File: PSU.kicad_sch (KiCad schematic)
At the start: 1 part, among them U1 IRM-01-3.3

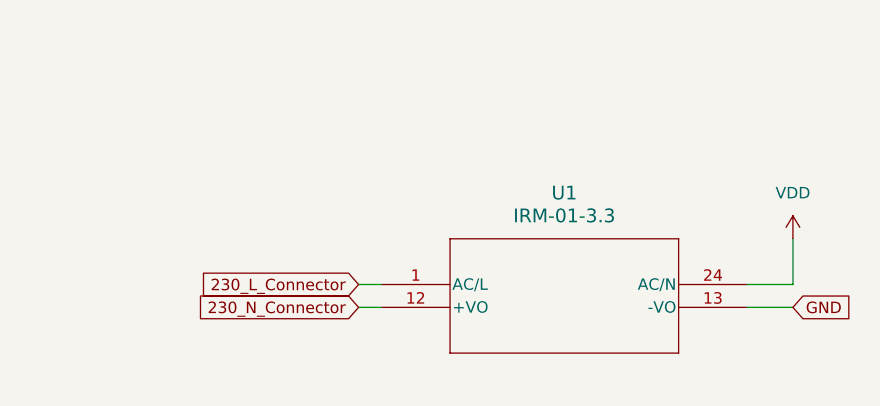
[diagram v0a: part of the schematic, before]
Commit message: Dodanie footprintów
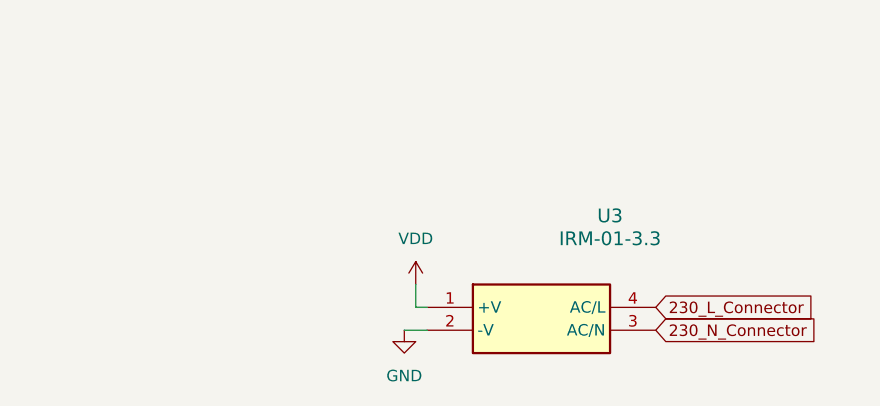
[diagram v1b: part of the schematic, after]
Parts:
- U3: renamed from U1; footprint IRM02_MWU -> Sterownik_roletyLibrary:IRM015; symbol IRM-01-3.3:IRM-01-3.3 -> IRM-01-3_3:IRM-01-3.3; Height (none) -> 15; Manufacturer_Name (none) -> Mean Well; Manufacturer_Part_Number (none) -> IRM-01-3.3; Mouser Part Number (none) -> 709-IRM01-3.3; Mouser Price/Stock (none) -> https://www.mouser.co.uk/ProductDetail/MEAN-WELL/IRM-01-3.3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
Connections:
- net 230_L_Connector: now also U3.4 (AC/L); no longer U3.1 (AC/L)
- net 230_N_Connector: now also U3.3 (AC/N); no longer U3.12 (+VO)
- net GND: now also U3.2 (-V); no longer U3.13 (-VO)
- net VDD: now also U3.1 (+V); no longer U3.24 (AC/N)
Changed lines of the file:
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@@
 	(wire
 		(pts
-			(xy 158.75 91.44) (xy 163.83 91.44)
+			(xy 123.19 93.98) (xy 121.92 93.98)
 		)
 		(stroke
@@
 	(wire
 		(pts
-			(xy 115.57 91.44) (xy 118.11 91.44)
+			(xy 121.92 93.98) (xy 121.92 91.44)
 		)
 		(stroke
@@
 	(wire
 		(pts
-			(xy 163.83 91.44) (xy 163.83 86.36)
-		)
-		(stroke
-			(width 0)
-			(type default)
-		)
-	)
-	(wire
-		(pts
-			(xy 115.57 93.98) (xy 118.11 93.98)
-		)
-		(stroke
-			(width 0)
-			(type default)
-		)
-	)
-	(wire
-		(pts
-			(xy 163.83 93.98) (xy 158.75 93.98)
+			(xy 120.65 96.52) (xy 123.19 96.52)
 		)
 		(stroke
@@
 		)
 	)
-	(global_label "GND"
+	(global_label "230_N_Connector"
 		(shape input)
-		(at 163.83 93.98 0)
+		(at 148.59 96.52 0)
 		(fields_autoplaced yes)
 		(effects
@@
 		)
 		(property "Intersheetrefs" "${INTERSHEET_REFS}"
-			(at 170.6857 93.98 0)
+			(at 168.0245 96.52 0)
 			(effects
 				(font
@@
 		)
 	)
-	(global_label "230_N_Connector"
+	(global_label "230_L_Connector"
 		(shape input)
-		(at 115.57 93.98 180)
+		(at 148.59 93.98 0)
 		(fields_autoplaced yes)
 		(effects
@@
 				(size 1.27 1.27)
 			)
-			(justify right)
+			(justify left)
 		)
 		(property "Intersheetrefs" "${INTERSHEET_REFS}"
-			(at 96.1355 93.98 0)
-			(effects
-				(font
-					(size 1.27 1.27)
-				)
-				(justify right)
-				(hide yes)
-			)
-		)
-	)
-	(global_label "230_L_Connector"
-		(shape input)
-		(at 115.57 91.44 180)
-		(fields_autoplaced yes)
-		(effects
-			(font
-				(size 1.27 1.27)
-			)
-			(justify right)
-		)
-		(property "Intersheetrefs" "${INTERSHEET_REFS}"
-			(at 96.4379 91.44 0)
-			(effects
-				(font
-					(size 1.27 1.27)
-				)
-				(justify right)
+			(at 167.7221 93.98 0)
+			(effects
+				(font
+					(size 1.27 1.27)
+				)
+				(justify left)
 				(hide yes)
 			)
@@
 	(symbol
 		(lib_id "power:VDD")
-		(at 163.83 86.36 0)
+		(at 121.92 91.44 0)
 		(unit 1)
 		(exclude_from_sim no)
@@
 		(dnp no)
 		(fields_autoplaced yes)
-		(property "Reference" "#PWR09"
-			(at 163.83 90.17 0)
+		(property "Reference" "#PWR015"
+			(at 121.92 95.25 0)
 			(effects
 				(font
@@
 		)
 		(property "Value" "VDD"
-			(at 163.83 81.28 0)
+			(at 121.92 86.36 0)
 			(effects
 				(font
@@
 		)
 		(property "Footprint" ""
-			(at 163.83 86.36 0)
+			(at 121.92 91.44 0)
 			(effects
 				(font
@@
 		)
 		(property "Datasheet" ""
-			(at 163.83 86.36 0)
+			(at 121.92 91.44 0)
 			(effects
 				(font
@@
 		)
 		(property "Description" "Power symbol creates a global label with name \"VDD\""
-			(at 163.83 86.36 0)
+			(at 121.92 91.44 0)
 			(effects
 				(font
@@
 			(project ""
 				(path "/e63e39d7-6ac0-4ffd-8aa3-1841a4541b55/d9942cb9-a0c0-49db-85f2-749386b323ae"
-					(reference "#PWR09")
+					(reference "#PWR015")
 					(unit 1)
 				)
@@
 	)
 	(symbol
-		(lib_id "IRM-01-3.3:IRM-01-3.3")
-		(at 118.11 91.44 0)
+		(lib_id "power:GND")
+		(at 120.65 96.52 0)
 		(unit 1)
 		(exclude_from_sim no)
@@
 		(dnp no)
 		(fields_autoplaced yes)
-		(property "Reference" "U1"
-			(at 138.43 81.28 0)
+		(property "Reference" "#PWR014"
+			(at 120.65 102.87 0)
+			(effects
+				(font
+					(size 1.27 1.27)
+				)
+				(hide yes)
+			)
+		)
+		(property "Value" "GND"
+			(at 120.65 101.6 0)
+			(effects
+				(font
+					(size 1.27 1.27)
+				)
+			)
+		)
+		(property "Footprint" ""
+			(at 120.65 96.52 0)
+			(effects
+				(font
+					(size 1.27 1.27)
+				)
+				(hide yes)
+			)
+		)
+		(property "Datasheet" ""
+			(at 120.65 96.52 0)
+			(effects
+				(font
+					(size 1.27 1.27)
+				)
+				(hide yes)
+			)
+		)
+		(property "Description" "Power symbol creates a global label with name \"GND\" , ground"
+			(at 120.65 96.52 0)
+			(effects
+				(font
+					(size 1.27 1.27)
+				)
+				(hide yes)
+			)
+		)
+		(pin "1"
+		)
+		(instances
+			(project ""
+				(path "/e63e39d7-6ac0-4ffd-8aa3-1841a4541b55/d9942cb9-a0c0-49db-85f2-749386b323ae"
+					(reference "#PWR014")
+					(unit 1)
+				)
+			)
+		)
+	)
+	(symbol
+		(lib_id "IRM-01-3_3:IRM-01-3.3")
+		(at 123.19 93.98 0)
+		(unit 1)
+		(exclude_from_sim no)
+		(in_bom yes)
+		(on_board yes)
+		(dnp no)
+		(fields_autoplaced yes)
+		(property "Reference" "U3"
+			(at 143.51 83.82 0)
 			(effects
 				(font
@@
 		)
 		(property "Value" "IRM-01-3.3"
-			(at 138.43 83.82 0)
+			(at 143.51 86.36 0)
 			(effects
 				(font
@@
 			)
 		)
-		(property "Footprint" "IRM02_MWU"
-			(at 118.11 91.44 0)
+		(property "Footprint" "Sterownik_roletyLibrary:IRM015"
+			(at 123.19 93.98 0)
 			(effects
 				(font
@@
 			)
 		)
-		(property "Datasheet" "IRM-01-3.3"
-			(at 118.11 91.44 0)
+		(property "Datasheet" "https://www.meanwell.com/Upload/PDF/IRM-01/IRM-01-SPEC.PDF"
+			(at 123.19 93.98 0)
 			(effects
 				(font
@@
 			)
 		)
-		(property "Description" ""
-			(at 118.11 91.44 0)
-			(effects
-				(font
-					(size 1.27 1.27)
-				)
-				(hide yes)
-			)
-		)
-		(pin "13"
-		)
-		(pin "24"
-		)
-		(pin "12"
+		(property "Description" "Power Supply Encapsulated PCB 3.3V 1W"
+			(at 123.19 93.98 0)
+			(effects
+				(font
+					(size 1.27 1.27)
+				)
+				(hide yes)
+			)
+		)
+		(property "Height" "15"
+			(at 144.78 488.9 0)
+			(effects
+				(font
+					(size 1.27 1.27)
+				)
+				(justify left top)
+				(hide yes)
+			)
+		)
+		(property "Mouser Part Number" "709-IRM01-3.3"
+			(at 144.78 588.9 0)
+			(effects
+				(font
+					(size 1.27 1.27)
+				)
+				(justify left top)
+				(hide yes)
+			)
+		)
+		(property "Mouser Price/Stock" "https://www.mouser.co.uk/ProductDetail/MEAN-WELL/IRM-01-3.3?qs=C9r8PV%2F%252BoWPYMhpLuTFr9w%3D%3D"
+			(at 144.78 688.9 0)
+			(effects
+				(font
+					(size 1.27 1.27)
+				)
+				(justify left top)
+				(hide yes)
+			)
+		)
+		(property "Manufacturer_Name" "Mean Well"
+			(at 144.78 788.9 0)
+			(effects
+				(font
+					(size 1.27 1.27)
+				)
+				(justify left top)
+				(hide yes)
+			)
+		)
+		(property "Manufacturer_Part_Number" "IRM-01-3.3"
+			(at 144.78 888.9 0)
+			(effects
+				(font
+					(size 1.27 1.27)
+				)
+				(justify left top)
+				(hide yes)
+			)
+		)
+		(pin "2"
+		)
+		(pin "3"
+		)
+		(pin "4"
 		)
 		(pin "1"
@@
 			(project "sterownik_rolety_Zigbee"
 				(path "/e63e39d7-6ac0-4ffd-8aa3-1841a4541b55/d9942cb9-a0c0-49db-85f2-749386b323ae"
-					(reference "U1")
+					(reference "U3")
 					(unit 1)
 				)

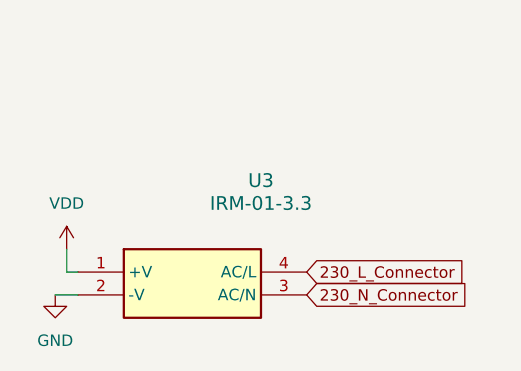
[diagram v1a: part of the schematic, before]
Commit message: początkowe rozłożenie na PCB
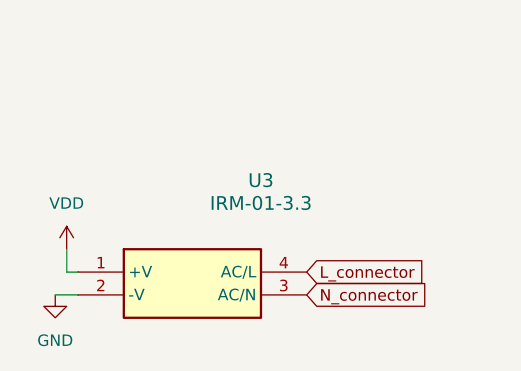
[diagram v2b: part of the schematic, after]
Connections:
- net 230_L_Connector renamed L_connector
- net 230_N_Connector renamed N_connector
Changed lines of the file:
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@@
 		)
 	)
-	(global_label "230_N_Connector"
+	(global_label "N_connector"
 		(shape input)
 		(at 148.59 96.52 0)
@@
 		)
 		(property "Intersheetrefs" "${INTERSHEET_REFS}"
-			(at 168.0245 96.52 0)
+			(at 163.247 96.52 0)
 			(effects
 				(font
@@
 		)
 	)
-	(global_label "230_L_Connector"
+	(global_label "L_connector"
 		(shape input)
 		(at 148.59 93.98 0)
@@
 		)
 		(property "Intersheetrefs" "${INTERSHEET_REFS}"
-			(at 167.7221 93.98 0)
+			(at 162.9446 93.98 0)
 			(effects
 				(font
